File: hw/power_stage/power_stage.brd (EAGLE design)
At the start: 100 x 100 mm, 54 parts, among them IC1H MIC4420M, IC1L MIC4429M, IC2H MIC4420M, IC2L MIC4429M

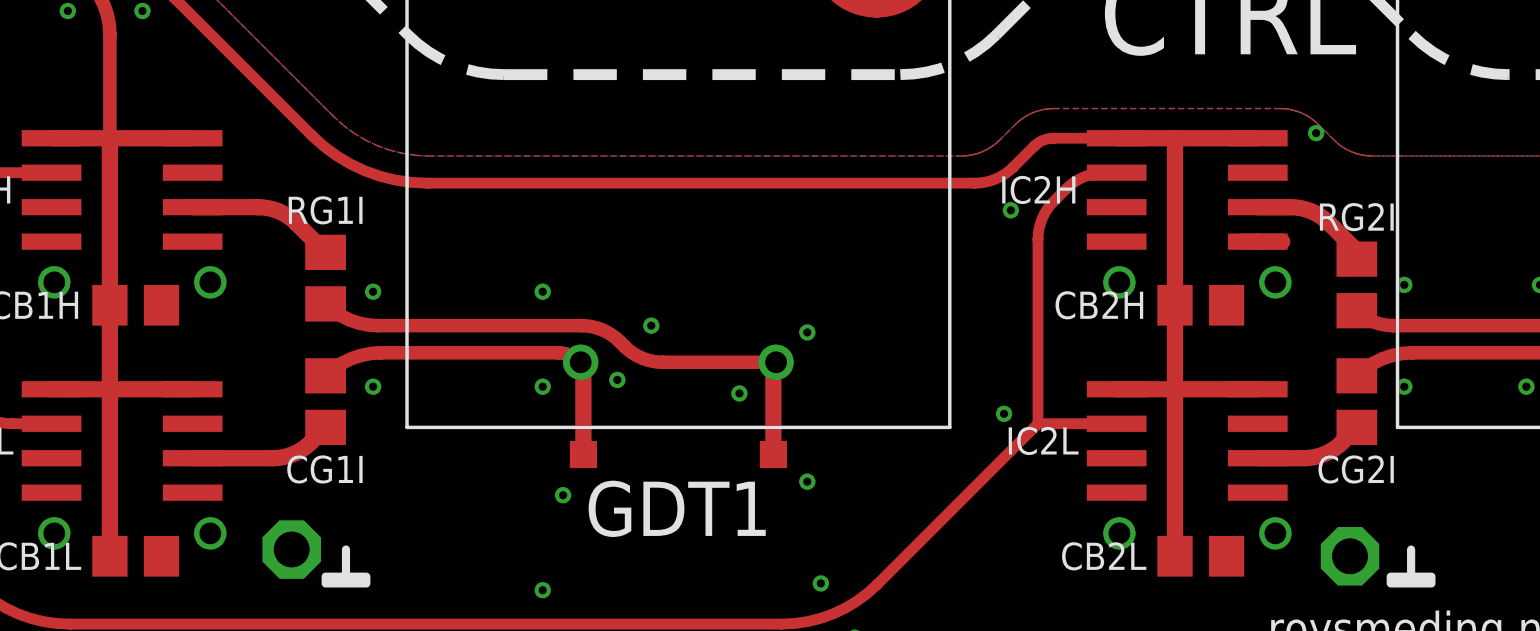
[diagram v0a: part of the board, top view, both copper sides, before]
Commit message: Fix unconnected output pin on gate driver ICs
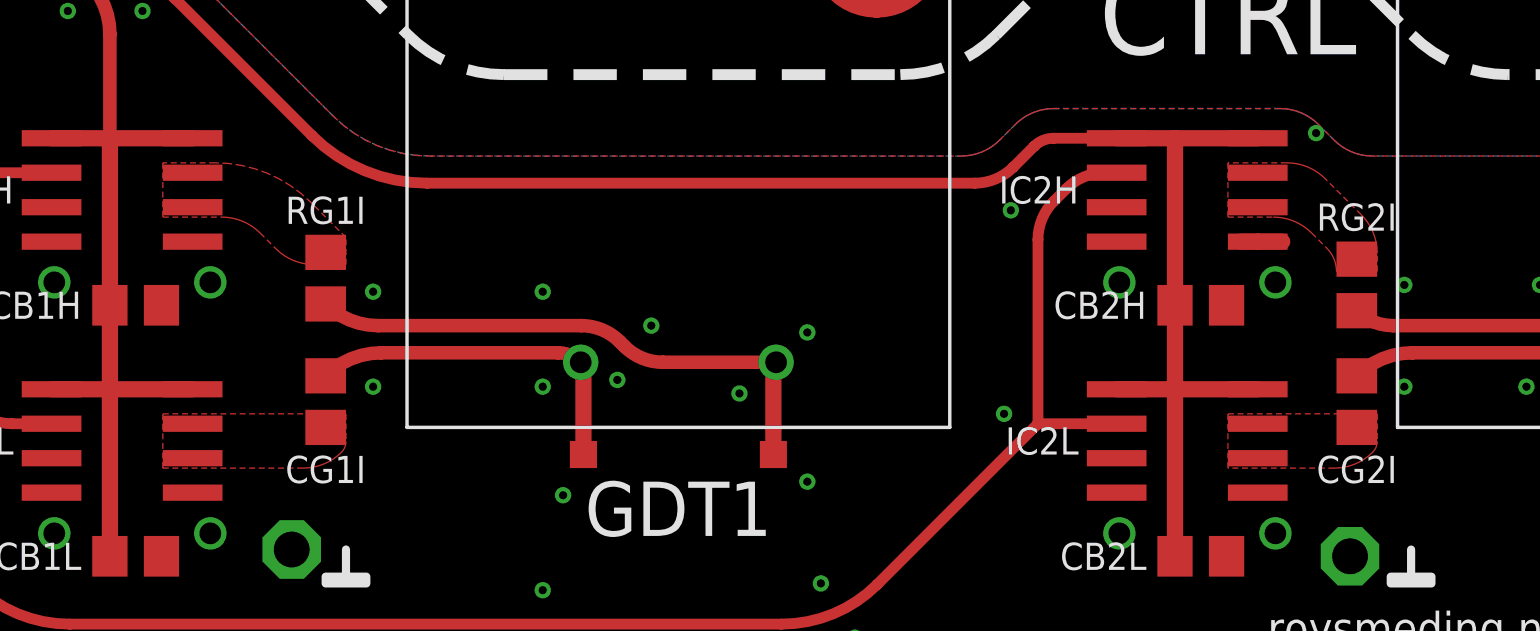
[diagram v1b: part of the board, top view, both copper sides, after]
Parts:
- IC1H, IC1L, IC2H, IC2L: device transistor-power:SO-08 -> induction-heater:SO-08
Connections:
- net N$2: now also IC1H.7
- net N$22: now also IC1L.7
- net N$25: now also IC2L.7
- net N$4: now also IC2H.7
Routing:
- net N$2: track 5.46 -> 0.00 mm
- net N$22: track 5.25 -> 0.00 mm
- net N$4: track 4.49 -> 0.00 mm
- net N$25: track 4.00 -> 0.00 mm
- added copper zone on layer 1, net N$2
- added copper zone on layer 1, net N$22
- added copper zone on layer 1, net N$25
- added copper zone on layer 1, net N$4
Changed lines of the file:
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@@
 <layer number="54" name="bGND_GNDA" color="1" fill="9" visible="no" active="no"/>
 <layer number="56" name="wert" color="7" fill="1" visible="no" active="no"/>
+<layer number="57" name="tCAD" color="7" fill="1" visible="no" active="no"/>
 <layer number="90" name="Modules" color="5" fill="1" visible="no" active="no"/>
 <layer number="91" name="Nets" color="2" fill="1" visible="no" active="no"/>
@@
 <layer number="108" name="tplace-old" color="10" fill="1" visible="yes" active="yes"/>
 <layer number="109" name="ref-old" color="11" fill="1" visible="yes" active="yes"/>
+<layer number="110" name="fp0" color="7" fill="1" visible="yes" active="yes"/>
+<layer number="111" name="LPC17xx" color="7" fill="1" visible="yes" active="yes"/>
+<layer number="112" name="tSilk" color="7" fill="1" visible="yes" active="yes"/>
+<layer number="113" name="IDFDebug" color="7" fill="1" visible="yes" active="yes"/>
 <layer number="116" name="Patch_BOT" color="9" fill="4" visible="yes" active="yes"/>
 <layer number="121" name="_tsilk" color="7" fill="1" visible="yes" active="yes"/>
 <layer number="122" name="_bsilk" color="7" fill="1" visible="yes" active="yes"/>
+<layer number="123" name="tTestmark" color="7" fill="1" visible="yes" active="yes"/>
+<layer number="124" name="bTestmark" color="7" fill="1" visible="yes" active="yes"/>
 <layer number="125" name="_tNames" color="7" fill="1" visible="yes" active="yes"/>
+<layer number="126" name="_bNames" color="7" fill="1" visible="yes" active="yes"/>
+<layer number="127" name="_tValues" color="7" fill="1" visible="yes" active="yes"/>
+<layer number="128" name="_bValues" color="7" fill="1" visible="yes" active="yes"/>
+<layer number="131" name="tAdjust" color="7" fill="1" visible="yes" active="yes"/>
+<layer number="132" name="bAdjust" color="7" fill="1" visible="yes" active="yes"/>
 <layer number="144" name="Drill_legend" color="7" fill="1" visible="yes" active="yes"/>
+<layer number="150" name="Notes" color="7" fill="1" visible="yes" active="yes"/>
 <layer number="151" name="HeatSink" color="7" fill="1" visible="yes" active="yes"/>
+<layer number="152" name="_bDocu" color="7" fill="1" visible="yes" active="yes"/>
+<layer number="153" name="FabDoc1" color="7" fill="1" visible="yes" active="yes"/>
+<layer number="154" name="FabDoc2" color="7" fill="1" visible="yes" active="yes"/>
+<layer number="155" name="FabDoc3" color="7" fill="1" visible="yes" active="yes"/>
 <layer number="199" name="Contour" color="7" fill="1" visible="yes" active="yes"/>
 <layer number="200" name="200bmp" color="1" fill="10" visible="yes" active="yes"/>
@@
 <layer number="223" name="223bmp" color="24" fill="1" visible="no" active="no"/>
 <layer number="224" name="224bmp" color="25" fill="1" visible="no" active="no"/>
+<layer number="248" name="Housing" color="7" fill="1" visible="yes" active="yes"/>
+<layer number="249" name="Edge" color="7" fill="1" visible="yes" active="yes"/>
 <layer number="250" name="Descript" color="3" fill="1" visible="no" active="no"/>
 <layer number="251" name="SMDround" color="12" fill="11" visible="no" active="no"/>
@@
 <attribute name="VALUE" x="69.635" y="76.04" size="1.27" layer="27" rot="R180"/>
 </element>
-<element name="IC1H" library="transistor-power" package="SO-08" value="MIC4420M" x="25" y="13.75" smashed="yes" rot="R270">
+<element name="IC1H" library="induction-heater" package="SO-08" value="MIC4420M" x="25" y="13.75" smashed="yes" rot="R270">
 <attribute name="NAME" x="21" y="13.75" size="1" layer="25" font="vector" ratio="15" align="center-right"/>
 </element>
-<element name="IC1L" library="transistor-power" package="SO-08" value="MIC4429M" x="25" y="4.5" smashed="yes" rot="R270">
+<element name="IC1L" library="induction-heater" package="SO-08" value="MIC4429M" x="25" y="4.5" smashed="yes" rot="R270">
 <attribute name="NAME" x="21" y="4.5" size="1" layer="25" font="vector" ratio="15" align="center-right"/>
 </element>
-<element name="IC2H" library="transistor-power" package="SO-08" value="MIC4420M" x="64.25" y="13.75" smashed="yes" rot="R270">
+<element name="IC2H" library="induction-heater" package="SO-08" value="MIC4420M" x="64.25" y="13.75" smashed="yes" rot="R270">
 <attribute name="NAME" x="60.25" y="13.75" size="1" layer="25" font="vector" ratio="15" align="center-right"/>
 </element>
-<element name="IC2L" library="transistor-power" package="SO-08" value="MIC4429M" x="64.25" y="4.5" smashed="yes" rot="R270">
+<element name="IC2L" library="induction-heater" package="SO-08" value="MIC4429M" x="64.25" y="4.5" smashed="yes" rot="R270">
 <attribute name="NAME" x="60.25" y="4.5" size="1" layer="25" font="vector" ratio="15" align="center-right"/>
 </element>
@@
 <contactref element="IC1L" pad="6"/>
 <contactref element="CG1I" pad="2"/>
-<wire x1="27.6" y1="3.865" x2="30.546140625" y2="3.865" width="0.6" layer="1"/>
-<wire x1="30.546140625" y1="3.865" x2="31.97286875" y2="4.4634125" width="0.6" layer="1" curve="45.509283"/>
-<wire x1="31.97286875" y1="4.4634125" x2="32.5" y2="5" width="0.6" layer="1"/>
+<contactref element="IC1L" pad="7"/>
+<polygon width="0.2" layer="1" thermals="no">
+<vertex x="26.5" y="5.5"/>
+<vertex x="33.25" y="5.5"/>
+<vertex x="33.25" y="4.48223125" curve="-45"/>
+<vertex x="33.0857875" y="4.0857875" curve="-45.00009"/>
+<vertex x="31.671571875" y="3.5"/>
+<vertex x="26.5" y="3.5"/>
+</polygon>
 </signal>
 <signal name="N$20" class="2">
@@
 <contactref element="IC2L" pad="6"/>
 <contactref element="CG2I" pad="2"/>
-<wire x1="66.85" y1="3.865" x2="68.546140625" y2="3.865" width="0.6" layer="1"/>
-<wire x1="68.546140625" y1="3.865" x2="69.97286875" y2="4.4634125" width="0.6" layer="1" curve="45.509283"/>
-<wire x1="69.97286875" y1="4.4634125" x2="70.5" y2="5" width="0.6" layer="1"/>
+<contactref element="IC2L" pad="7"/>
+<polygon width="0.2" layer="1" thermals="no">
+<vertex x="65.75" y="5.5"/>
+<vertex x="71.25" y="5.5"/>
+<vertex x="71.25" y="4.48223125" curve="-45"/>
+<vertex x="71.0857875" y="4.0857875" curve="-45.00009"/>
+<vertex x="69.671571875" y="3.5"/>
+<vertex x="65.75" y="3.5"/>
+</polygon>
 </signal>
 <signal name="GND" class="2">
@@
 <contactref element="JP1" pad="4"/>
 <contactref element="JP2" pad="1"/>
-<polygon width="0.5" layer="1" isolate="0.5">
+<polygon width="0.5" layer="1" isolate="0.5" rank="2">
 <vertex x="-1.25" y="-3.25"/>
 <vertex x="-1.25" y="23.75" curve="-90"/>
@@
 <contactref element="RG1I" pad="1"/>
 <contactref element="IC1H" pad="6"/>
-<wire x1="27.6" y1="13.115" x2="30.006571875" y2="13.115" width="0.6" layer="1"/>
-<wire x1="30.006571875" y1="13.115" x2="31.4207875" y2="12.5292125" width="0.6" layer="1" curve="-45.000063"/>
-<wire x1="31.4207875" y1="12.5292125" x2="32.5" y2="11.45" width="0.6" layer="1"/>
+<contactref element="IC1H" pad="7"/>
+<polygon width="0.2" layer="1" thermals="no">
+<vertex x="26.5" y="14.75"/>
+<vertex x="26.5" y="12.75"/>
+<vertex x="28.671571875" y="12.75" curve="-45.000063"/>
+<vertex x="30.0857875" y="12.1642125"/>
+<vertex x="30.6642125" y="11.5857875" curve="45.00009"/>
+<vertex x="32.078428125" y="11"/>
+<vertex x="33.25" y="11"/>
+<vertex x="33.25" y="12"/>
+<vertex x="31.964465625" y="13.285534375" curve="45"/>
+<vertex x="28.42893125" y="14.75"/>
+</polygon>
 </signal>
 <signal name="N$4">
 <contactref element="IC2H" pad="6"/>
 <contactref element="RG2I" pad="1"/>
-<wire x1="66.85" y1="13.115" x2="68.056571875" y2="13.115" width="0.6" layer="1"/>
-<wire x1="68.056571875" y1="13.115" x2="69.4707875" y2="12.5292125" width="0.6" layer="1" curve="-45.000063"/>
-<wire x1="69.4707875" y1="12.5292125" x2="70.5" y2="11.5" width="0.6" layer="1"/>
-<wire x1="70.5" y1="11.2" x2="70.5" y2="11.5" width="0.6" layer="1"/>
+<contactref element="IC2H" pad="7"/>
+<polygon width="0.2" layer="1" thermals="no">
+<vertex x="65.75" y="14.75"/>
+<vertex x="65.75" y="12.75"/>
+<vertex x="67.421571875" y="12.75" curve="-45.000063"/>
+<vertex x="68.8357875" y="12.1642125"/>
+<vertex x="69.396446875" y="11.603553125" curve="-45"/>
+<vertex x="69.75" y="10.75"/>
+<vertex x="71.25" y="10.75"/>
+<vertex x="71.25" y="11.421571875" curve="45.000063"/>
+<vertex x="70.6642125" y="12.8357875"/>
+<vertex x="69.3357875" y="14.1642125" curve="45.00009"/>
+<vertex x="67.921571875" y="14.75"/>
+</polygon>
 </signal>
 <signal name="N$5">

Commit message: why not
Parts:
- moved TP_GNDA 4.00 mm to (5.00, 0.00)
- moved OUT1 1.00 mm to (91.5, 32.8)
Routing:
- net N$20: track 69.9 -> 72.0 mm, vias 1 -> 0
- net V-: vias 0 -> 40
- net OUT2: vias 0 -> 30
- net OUT1: vias 0 -> 28
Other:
- board text removed: "AC1"
- board text removed: "AC2"
